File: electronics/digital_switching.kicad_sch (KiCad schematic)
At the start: 16 parts, among them J5 DB12, U10 BTS7006, U6 BTS7006, U7 BTS7006, U8 BTS7006, U9 BTS7006

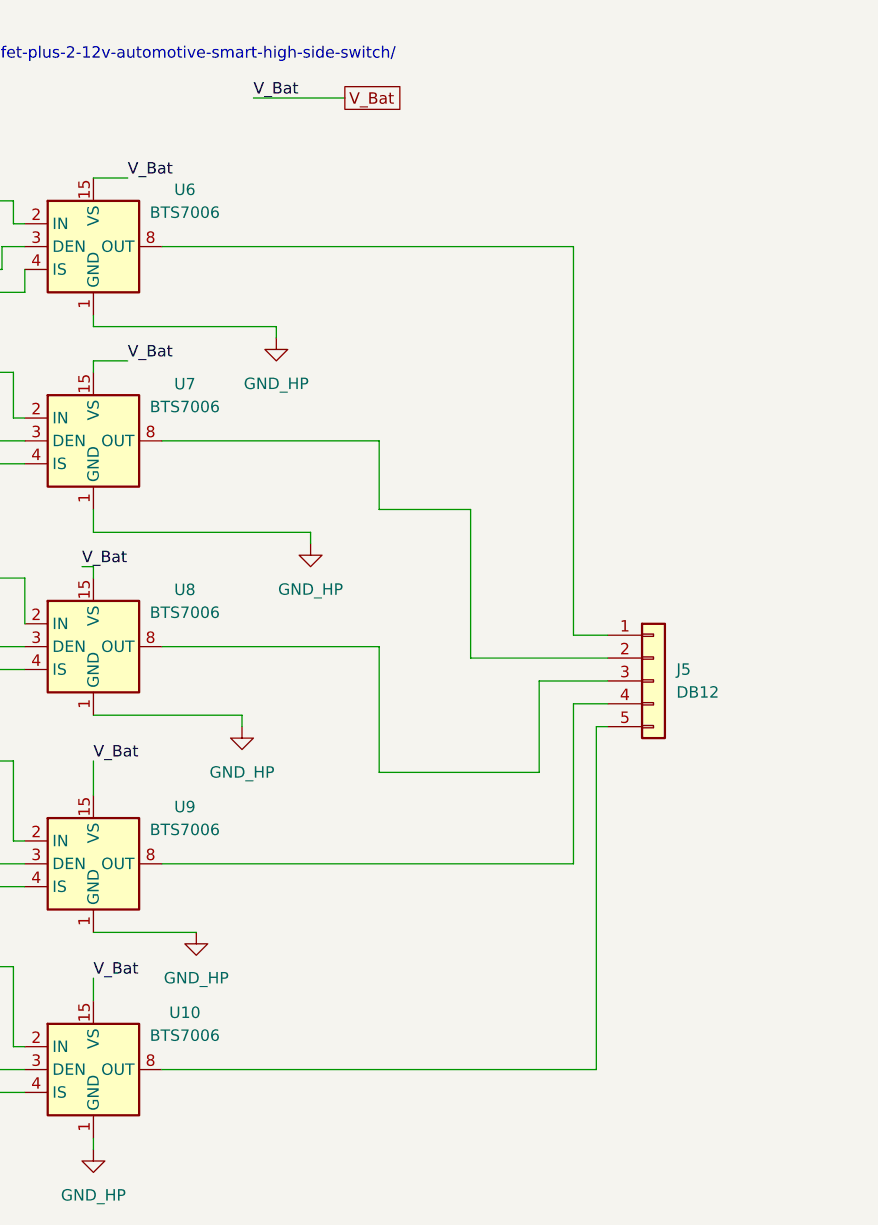
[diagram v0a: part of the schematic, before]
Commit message: capacitors added. universal dc/dc converters
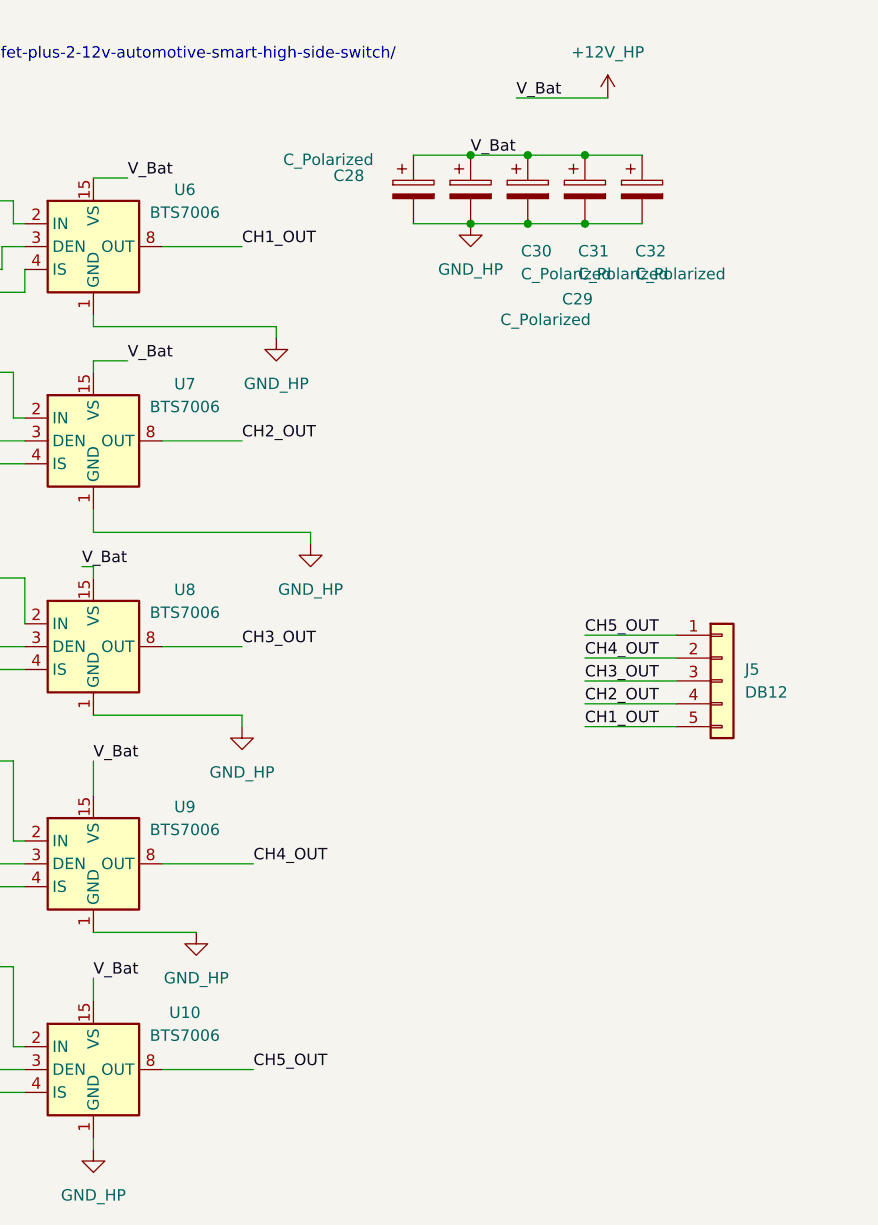
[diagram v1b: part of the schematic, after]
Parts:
- added C28, C29, C30, C31, C32: C_Polarized, Capacitor_THT:CP_Radial_D5.0mm_P2.50mm, symbol Device:C_Polarized
- R_DEN1, R_DEN2, R_DEN3, R_DEN4, R_DEN5, R_IN1, R_IN2, R_IN3, R_IN4, R_IN5: footprint Resistor_SMD:R_0805_2012Metric_Pad1.20x1.40mm_HandSolder -> Resistor_SMD:R_0805_2012Metric
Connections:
- net GND_HP: now also C28.2, C29.2, C30.2, C31.2, C32.2
- net CH2_OUT: now reaches U7.10 (OUT), U7.12 (OUT), U7.13 (OUT), U7.14 (OUT), U7.8 (OUT), U7.9 (OUT)
- net CH2_OUT: now also J5.4 (Pin_4); no longer J5.2 (Pin_2)
- net CH1_OUT: now reaches U6.10 (OUT), U6.12 (OUT), U6.13 (OUT), U6.14 (OUT), U6.8 (OUT), U6.9 (OUT)
- net CH1_OUT: now also J5.5 (Pin_5); no longer J5.1 (Pin_1)
- net CH4_OUT: now reaches U9.10 (OUT), U9.12 (OUT), U9.13 (OUT), U9.14 (OUT), U9.8 (OUT), U9.9 (OUT)
- net CH4_OUT: now also J5.2 (Pin_2); no longer J5.4 (Pin_4)
- net CH3_OUT: now reaches J5.3 (Pin_3), U8.10 (OUT), U8.12 (OUT), U8.13 (OUT), U8.14 (OUT), U8.8 (OUT), U8.9 (OUT)
- net CH5_OUT: now reaches U10.10 (OUT), U10.12 (OUT), U10.13 (OUT), U10.14 (OUT), U10.8 (OUT), U10.9 (OUT)
- net CH5_OUT: now also J5.1 (Pin_1); no longer J5.5 (Pin_5)
- net V_Bat renamed +12V_HP
- net +12V_HP: now also C28.1, C29.1, C30.1, C31.1, C32.1
